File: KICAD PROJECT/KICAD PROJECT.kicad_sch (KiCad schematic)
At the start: 149 parts, among them IC1 TPS61032PWP, J1 AudioJack3_Ground_SwitchTR, J2 Conn_01x02_Pin, J4 Conn_01x08_Socket, J5 Conn_01x08_Socket, P1 USB_C_Plug_USB2.0, Q1 BC857, Q2 BSS84, Q3 BSS84, SW1 SW_Push, SW10 SW_Push, SW11 SW_Push, SW12 SW_Push, SW13 SW_Push, SW14 SW_Push, SW15 SW_Push, SW16 SW_Push, SW17 SW_Push, SW18 SW_Push, SW19 SW_Push, SW2 SW_Push, SW20 SW_Push, SW21 SW_Push, SW22 SW_Push, SW23 SW_Push, SW24 SW_Push, SW25 SW_Push, SW26 SW_Push, SW27 SW_Push, SW28 SW_Push, SW29 SW_Push, SW3 SW_Push, SW30 SW_Push, SW31 SW_Push, SW32 SW_Push, SW33 SW_Push, SW34 SW_Push, SW35 SW_Push, SW37 SW_Push, SW38 SW_Push, SW39 SW_Push, SW4 SW_Push, SW40 SW_Push, SW41 SW_Push, SW42 SW_Push, SW43 SW_Push, SW44 SW_SPDT, SW5 SW_Push, SW6 SW_Push, SW7 SW_Push, SW8 SW_Push, SW9 SW_Push, U1 PCM5102A, U2 Raspberry pi Zero 2 w, U3 RP2040-ZERO, U4 PAM8302AAD, U8 MCP73833-xxx-MF

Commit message: Updates and gerbers
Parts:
- added R16: 4.5k, Resistor_SMD:R_0603_1608Metric_Pad0.98x0.95mm_HandSolder, symbol Device:R
- IC1: footprint Package_SO:HTSSOP-16-1EP_4.4x5mm_P0.65mm_EP3.4x5mm_Mask2.66x2.46mm_ThermalVias -> Package_SO:HTSSOP-16-1EP_4.4x5mm_P0.65mm_EP3.4x5mm_Mask2.66x2.46mm
- R1: value 1k -> 2K
- R2: value 1k -> 4.5k
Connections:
- net +5V: now also R2.1, R16.1
- net GND: now also U8.5 (V_{SS}); no longer C21.2
- net SCL: now also R16.2
- net SDA: now also R2.2
- net at C20.1, R14.2: no longer R15.2
- net at R3.1: now also R1.2; no longer R2.1
- new net: C21.2, R15.2
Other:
- moved on the sheet: R14

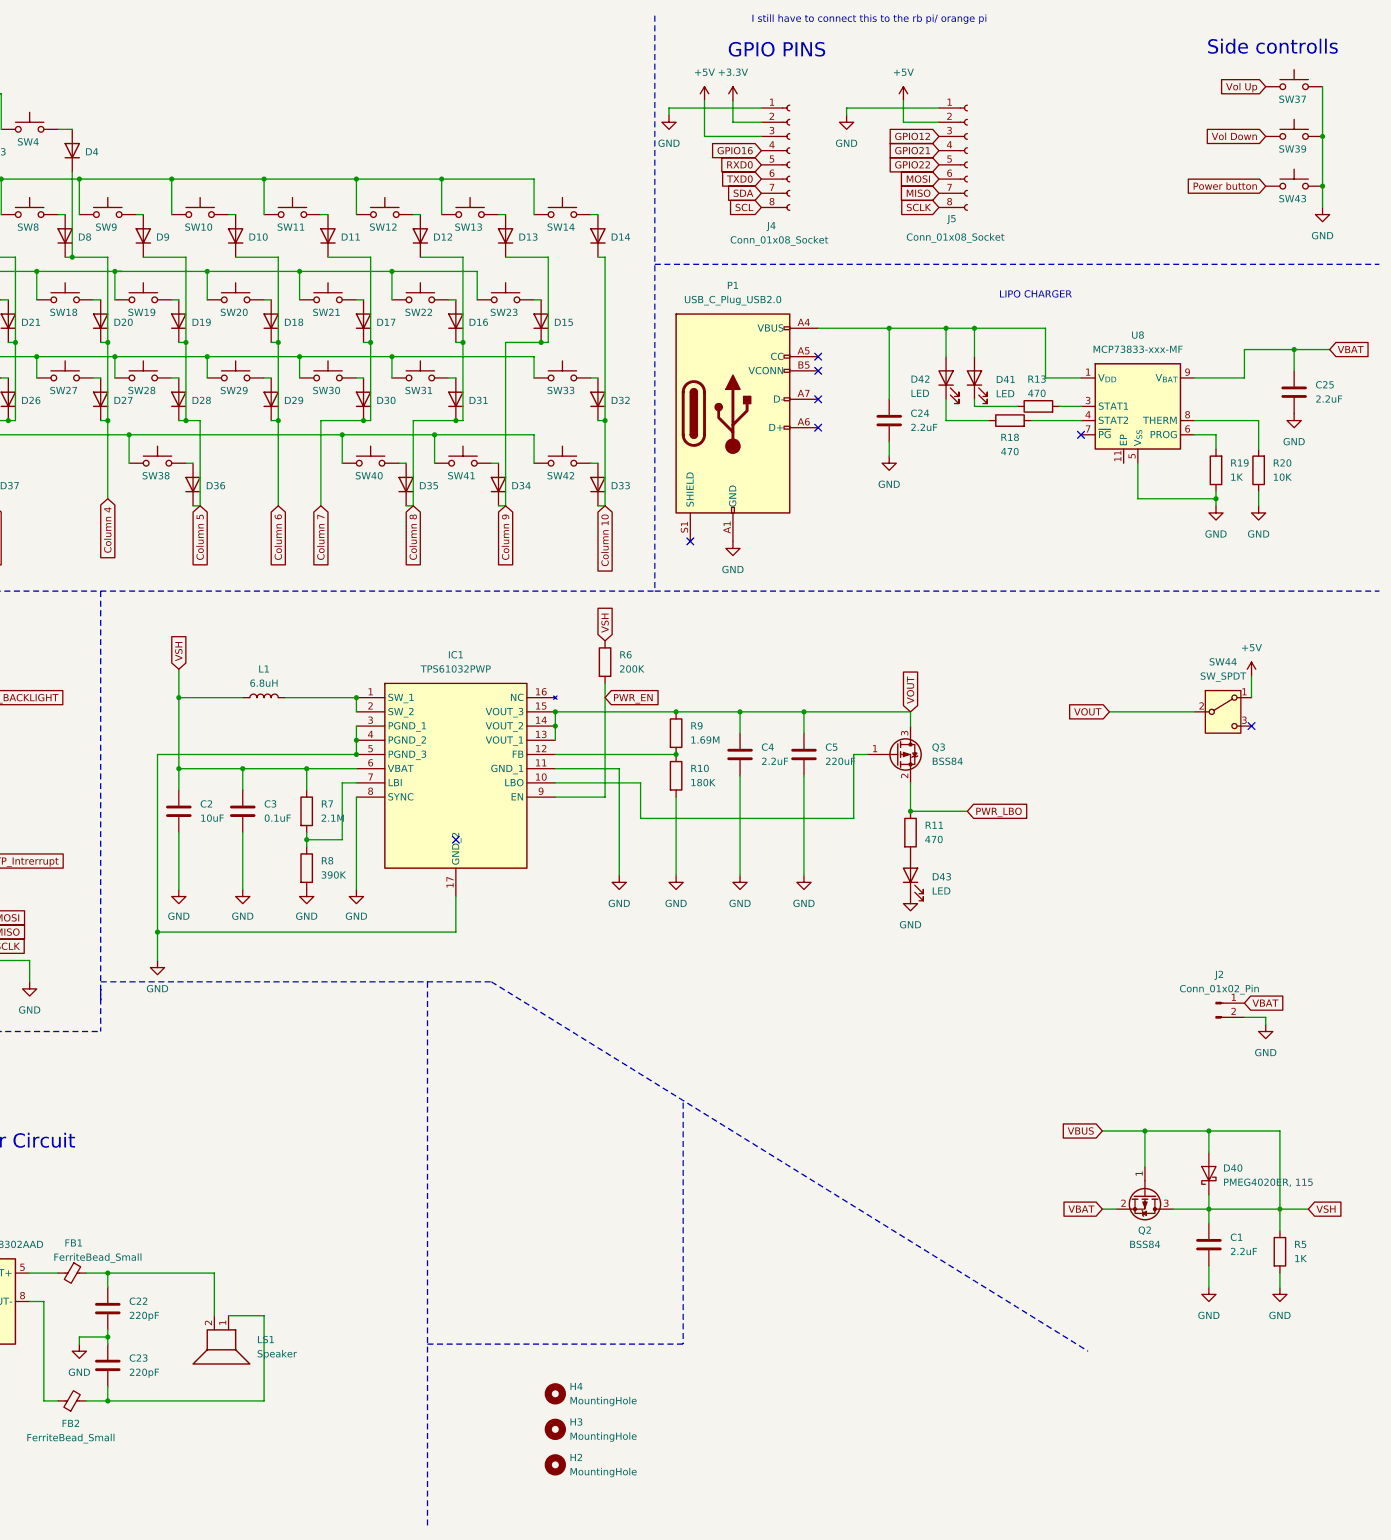
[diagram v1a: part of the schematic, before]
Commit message: Stl Files + Render +Organized Repo
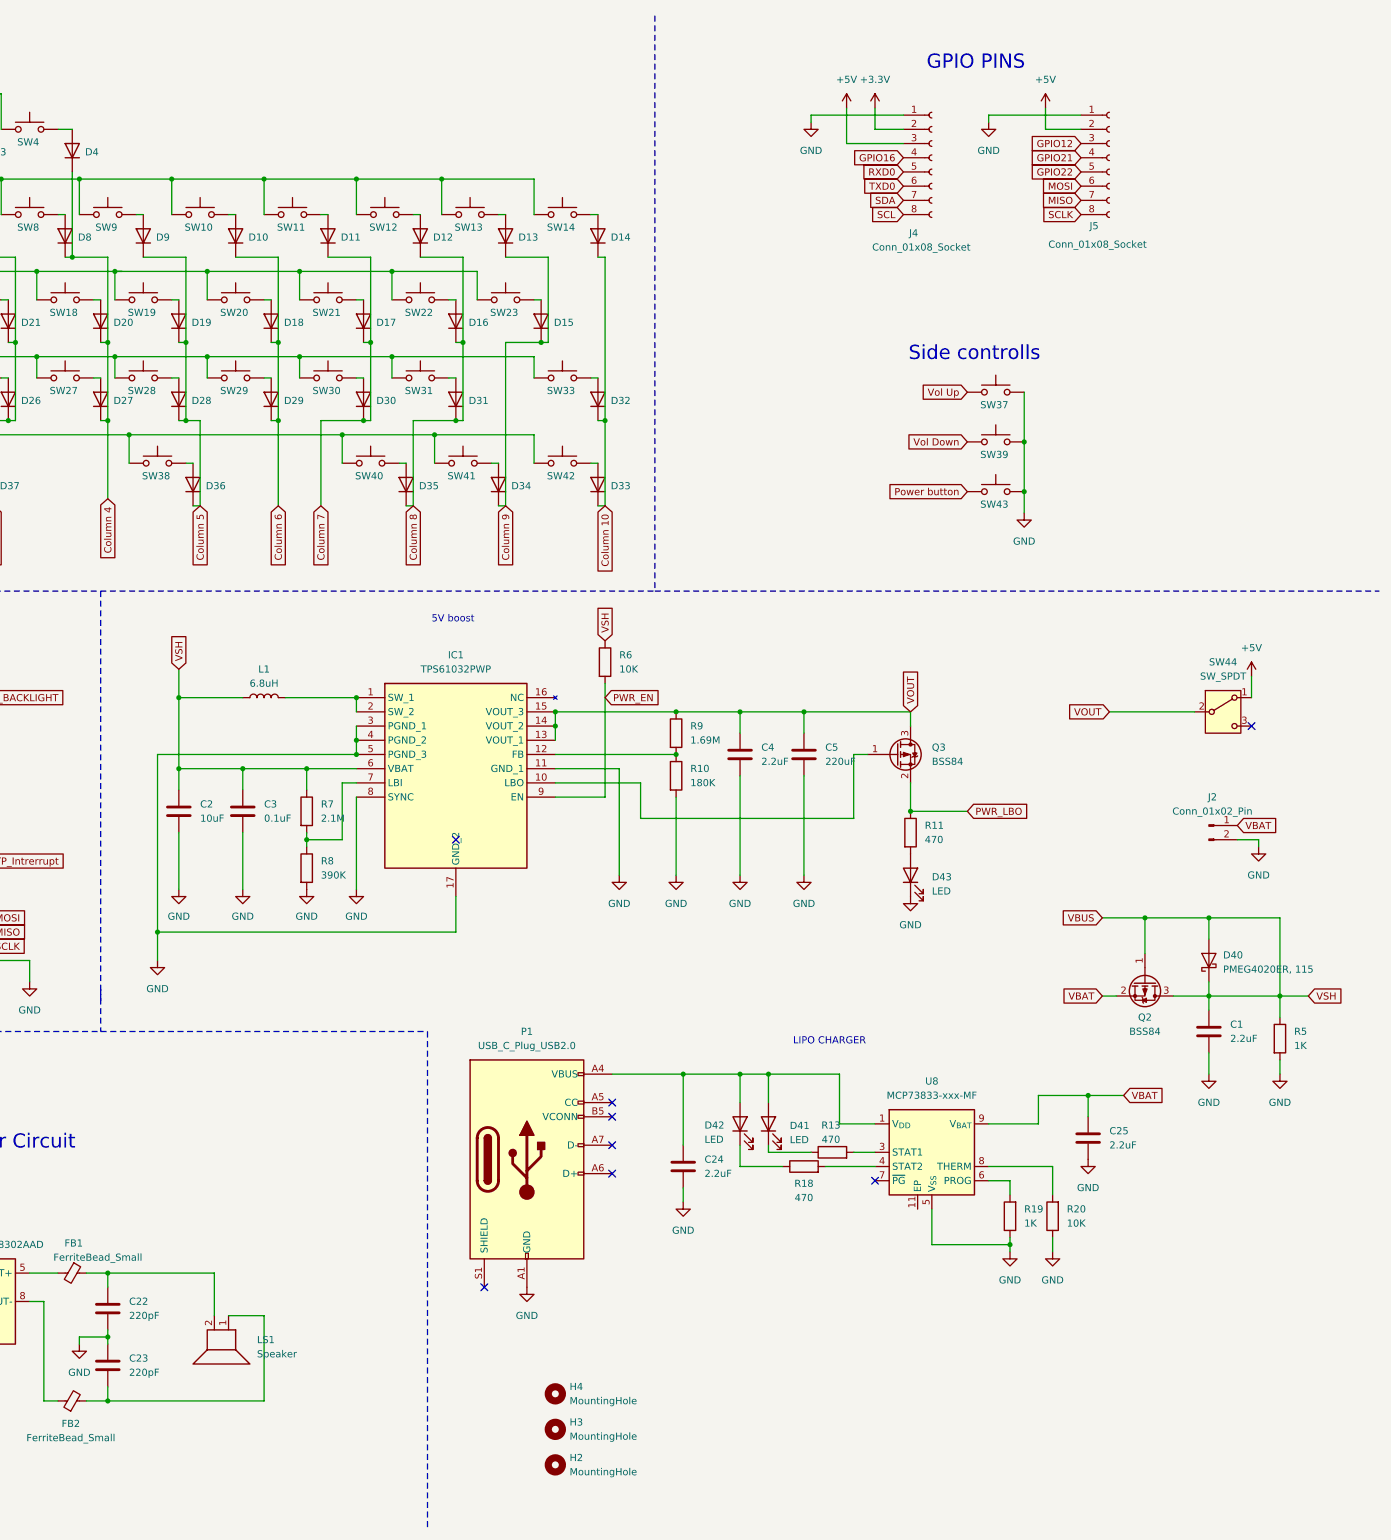
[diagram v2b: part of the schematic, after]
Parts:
- R6: value 200K -> 10K
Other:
- note added: "5V boost"
- note removed: "I still have to connect this to the rb pi/ orange pi"
- company: (none) -> Istratie Stefan
- moved on the sheet: C1, C24, C25, D40, D41, D42, J2, J4, J5, P1, Q2, R13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
